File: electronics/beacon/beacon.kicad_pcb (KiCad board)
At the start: 2 copper layers, 28 x 3.5 mm, 12 parts, among them Q1 Q_NMOS_GSD, U1 ATTINY45-20XUR, U2 TPS70928DBV

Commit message: Finalize beacon schematic for initial run
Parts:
- C1: value 1uF -> 1u
- C2: value 22uF -> 22u
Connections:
- net /Rail1 renamed Net-(D2-Pad2)
- net /Rail2 renamed Net-(D2-Pad3)
- net VCC renamed Net-(C1-Pad1)
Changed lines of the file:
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@@
   )
   (net 0 "")
-  (net 1 VCC)
-  (net 2 GND)
-  (net 3 +2V8)
-  (net 4 "Net-(D1-Pad2)")
-  (net 5 "Net-(D1-Pad1)")
-  (net 6 /Rail1)
-  (net 7 /Rail2)
-  (net 8 "Net-(Q1-Pad1)")
-  (net 9 /~RST)
-  (net 10 /MISO)
-  (net 11 /MOSI)
-  (net 12 /SCK)
-  (net 13 "Net-(U2-Pad3)")
-  (net 14 "Net-(U2-Pad4)")
-  (net 15 /PB3)
-  (net 16 /PB4)
+  (net 1 GND)
+  (net 2 +2V8)
+  (net 3 "Net-(D1-Pad2)")
+  (net 4 "Net-(D1-Pad1)")
+  (net 5 "Net-(Q1-Pad1)")
+  (net 6 /~RST)
+  (net 7 /MISO)
+  (net 8 /MOSI)
+  (net 9 /SCK)
+  (net 10 "Net-(U2-Pad3)")
+  (net 11 "Net-(U2-Pad4)")
+  (net 12 /PB3)
+  (net 13 /PB4)
+  (net 14 "Net-(C1-Pad1)")
+  (net 15 "Net-(D2-Pad2)")
+  (net 16 "Net-(D2-Pad3)")
   (net_class Default "This is the default net class."
     (clearance 0.2)
@@
     (add_net /PB3)
     (add_net /PB4)
-    (add_net /Rail1)
-    (add_net /Rail2)
     (add_net /SCK)
     (add_net /~RST)
     (add_net GND)
+    (add_net "Net-(C1-Pad1)")
     (add_net "Net-(D1-Pad1)")
     (add_net "Net-(D1-Pad2)")
+    (add_net "Net-(D2-Pad2)")
+    (add_net "Net-(D2-Pad3)")
     (add_net "Net-(Q1-Pad1)")
     (add_net "Net-(U2-Pad3)")
     (add_net "Net-(U2-Pad4)")
-    (add_net VCC)
   )
   (module Housings_SSOP:TSSOP-8_4.4x3mm_Pitch0.65mm (layer B.Cu)
@@
     (fp_line (start -2.325 1.525) (end -3.675 1.525) (layer B.SilkS) (width 0.15))
     (pad 1 smd rect (at -2.95 0.975) (size 1.45 0.45) (layers B.Cu B.Paste B.Mask)
-      (net 9 /~RST))
+      (net 6 /~RST))
     (pad 2 smd rect (at -2.95 0.325) (size 1.45 0.45) (layers B.Cu B.Paste B.Mask)
-      (net 15 /PB3))
+      (net 12 /PB3))
     (pad 3 smd rect (at -2.95 -0.325) (size 1.45 0.45) (layers B.Cu B.Paste B.Mask)
-      (net 16 /PB4))
+      (net 13 /PB4))
     (pad 4 smd rect (at -2.95 -0.975) (size 1.45 0.45) (layers B.Cu B.Paste B.Mask)
-      (net 2 GND))
+      (net 1 GND))
     (pad 5 smd rect (at 2.95 -0.975) (size 1.45 0.45) (layers B.Cu B.Paste B.Mask)
-      (net 11 /MOSI))
+      (net 8 /MOSI))
     (pad 6 smd rect (at 2.95 -0.325) (size 1.45 0.45) (layers B.Cu B.Paste B.Mask)
-      (net 10 /MISO))
+      (net 7 /MISO))
     (pad 7 smd rect (at 2.95 0.325) (size 1.45 0.45) (layers B.Cu B.Paste B.Mask)
-      (net 12 /SCK))
+      (net 9 /SCK))
     (pad 8 smd rect (at 2.95 0.975) (size 1.45 0.45) (layers B.Cu B.Paste B.Mask)
-      (net 3 +2V8))
+      (net 2 +2V8))
     (model Housings_SSOP.3dshapes/TSSOP-8_4.4x3mm_Pitch0.65mm.wrl
       (at (xyz 0 0 0))
@@
     (fp_line (start -0.5 0.675) (end 0.5 0.675) (layer B.SilkS) (width 0.15))
     (pad 1 smd rect (at -1.1 0 270) (size 1.2 0.9) (layers B.Cu B.Paste B.Mask)
-      (net 3 +2V8))
+      (net 2 +2V8))
     (pad 2 smd rect (at 1.1 0 270) (size 1.2 0.9) (layers B.Cu B.Paste B.Mask)
-      (net 9 /~RST))
+      (net 6 /~RST))
     (model Resistors_SMD.3dshapes/R_0603_HandSoldering.wrl
       (at (xyz 0 0 0))
@@
       (effects (font (size 1 1) (thickness 0.15)))
     )
-    (fp_text value 1uF (at 0 1.5 270) (layer F.Fab)
+    (fp_text value 1u (at 0 1.5 270) (layer F.Fab)
       (effects (font (size 1 1) (thickness 0.15)))
     )
@@
     (fp_line (start 1.8 0.65) (end -1.8 0.65) (layer F.CrtYd) (width 0.05))
     (pad 1 smd rect (at -0.95 0 270) (size 1.2 0.75) (layers F.Cu F.Paste F.Mask)
-      (net 1 VCC))
+      (net 14 "Net-(C1-Pad1)"))
     (pad 2 smd rect (at 0.95 0 270) (size 1.2 0.75) (layers F.Cu F.Paste F.Mask)
-      (net 2 GND))
+      (net 1 GND))
     (model Capacitors_SMD.3dshapes/C_0603.wrl
       (at (xyz 0 0 0))
@@
       (effects (font (size 1 1) (thickness 0.15)))
     )
-    (fp_text value 22uF (at 0 1.5 270) (layer F.Fab)
+    (fp_text value 22u (at 0 1.5 270) (layer F.Fab)
       (effects (font (size 1 1) (thickness 0.15)))
     )
@@
     (fp_line (start 1.8 0.65) (end -1.8 0.65) (layer F.CrtYd) (width 0.05))
     (pad 1 smd rect (at -0.95 0 270) (size 1.2 0.75) (layers F.Cu F.Paste F.Mask)
-      (net 3 +2V8))
+      (net 2 +2V8))
     (pad 2 smd rect (at 0.95 0 270) (size 1.2 0.75) (layers F.Cu F.Paste F.Mask)
-      (net 2 GND))
+      (net 1 GND))
     (model Capacitors_SMD.3dshapes/C_0603.wrl
       (at (xyz 0 0 0))
@@
     (fp_line (start -1.45 -0.65) (end 1.45 -0.65) (layer F.CrtYd) (width 0.05))
     (pad 2 smd rect (at 0.8 0 270) (size 0.8 0.8) (layers F.Cu F.Paste F.Mask)
-      (net 4 "Net-(D1-Pad2)"))
+      (net 3 "Net-(D1-Pad2)"))
     (pad 1 smd rect (at -0.8 0 270) (size 0.8 0.8) (layers F.Cu F.Paste F.Mask)
-      (net 5 "Net-(D1-Pad1)"))
+      (net 4 "Net-(D1-Pad1)"))
     (model LEDs.3dshapes/LED_0603.wrl
       (at (xyz 0 0 0))
@@
     (fp_line (start -2.05 1.75) (end -2.05 -1.75) (layer F.CrtYd) (width 0.05))
     (pad 1 smd rect (at -1.1 -0.77 270) (size 1.2 1.4) (layers F.Cu F.Paste F.Mask)
-      (net 2 GND))
+      (net 1 GND))
     (pad 2 smd rect (at -1.1 0.95 270) (size 1 1.4) (layers F.Cu F.Paste F.Mask)
-      (net 6 /Rail1))
+      (net 15 "Net-(D2-Pad2)"))
     (pad 3 smd rect (at 1.1 0.95 270) (size 1 1.4) (layers F.Cu F.Paste F.Mask)
-      (net 7 /Rail2))
+      (net 16 "Net-(D2-Pad3)"))
     (pad 4 smd rect (at 1.1 -0.95 270) (size 1 1.4) (layers F.Cu F.Paste F.Mask)
-      (net 1 VCC))
+      (net 14 "Net-(C1-Pad1)"))
     (model TO_SOT_Packages_SMD.3dshapes/SOT-143.wrl
       (at (xyz 0 -0 0))
@@
     (fp_line (start 0.76 -1.58) (end -0.7 -1.58) (layer B.SilkS) (width 0.12))
     (pad 1 smd rect (at -1 0.95) (size 0.9 0.8) (layers B.Cu B.Paste B.Mask)
-      (net 8 "Net-(Q1-Pad1)"))
+      (net 5 "Net-(Q1-Pad1)"))
     (pad 2 smd rect (at -1 -0.95) (size 0.9 0.8) (layers B.Cu B.Paste B.Mask)
-      (net 2 GND))
+      (net 1 GND))
     (pad 3 smd rect (at 1 0) (size 0.9 0.8) (layers B.Cu B.Paste B.Mask)
-      (net 5 "Net-(D1-Pad1)"))
+      (net 4 "Net-(D1-Pad1)"))
     (model TO_SOT_Packages_SMD.3dshapes/SOT-23.wrl
       (at (xyz 0 0 0))
@@
     (fp_line (start -0.5 0.675) (end 0.5 0.675) (layer B.SilkS) (width 0.15))
     (pad 1 smd rect (at -1.1 0 270) (size 1.2 0.9) (layers B.Cu B.Paste B.Mask)
-      (net 10 /MISO))
+      (net 7 /MISO))
     (pad 2 smd rect (at 1.1 0 270) (size 1.2 0.9) (layers B.Cu B.Paste B.Mask)
-      (net 8 "Net-(Q1-Pad1)"))
+      (net 5 "Net-(Q1-Pad1)"))
     (model Resistors_SMD.3dshapes/R_0603_HandSoldering.wrl
       (at (xyz 0 0 0))
@@
     (fp_line (start -0.5 0.675) (end 0.5 0.675) (layer B.SilkS) (width 0.15))
     (pad 1 smd rect (at -1.1 0 90) (size 1.2 0.9) (layers B.Cu B.Paste B.Mask)
-      (net 8 "Net-(Q1-Pad1)"))
+      (net 5 "Net-(Q1-Pad1)"))
     (pad 2 smd rect (at 1.1 0 90) (size 1.2 0.9) (layers B.Cu B.Paste B.Mask)
-      (net 2 GND))
+      (net 1 GND))
     (model Resistors_SMD.3dshapes/R_0603_HandSoldering.wrl
       (at (xyz 0 0 0))
@@
     (fp_line (start -0.5 0.675) (end 0.5 0.675) (layer B.SilkS) (width 0.15))
     (pad 1 smd rect (at -1.1 0 270) (size 1.2 0.9) (layers B.Cu B.Paste B.Mask)
-      (net 3 +2V8))
+      (net 2 +2V8))
     (pad 2 smd rect (at 1.1 0 270) (size 1.2 0.9) (layers B.Cu B.Paste B.Mask)
-      (net 4 "Net-(D1-Pad2)"))
+      (net 3 "Net-(D1-Pad2)"))
     (model Resistors_SMD.3dshapes/R_0603_HandSoldering.wrl
       (at (xyz 0 0 0))
@@
     (fp_line (start 0.9 -1.55) (end 0.9 1.55) (layer F.Fab) (width 0.1))
     (pad 1 smd rect (at -1.1 -0.95) (size 1.06 0.65) (layers F.Cu F.Paste F.Mask)
-      (net 1 VCC))
+      (net 14 "Net-(C1-Pad1)"))
     (pad 2 smd rect (at -1.1 0) (size 1.06 0.65) (layers F.Cu F.Paste F.Mask)
-      (net 2 GND))
+      (net 1 GND))
     (pad 3 smd rect (at -1.1 0.95) (size 1.06 0.65) (layers F.Cu F.Paste F.Mask)
-      (net 13 "Net-(U2-Pad3)"))
+      (net 10 "Net-(U2-Pad3)"))
     (pad 4 smd rect (at 1.1 0.95) (size 1.06 0.65) (layers F.Cu F.Paste F.Mask)
-      (net 14 "Net-(U2-Pad4)"))
+      (net 11 "Net-(U2-Pad4)"))
     (pad 5 smd rect (at 1.1 -0.95) (size 1.06 0.65) (layers F.Cu F.Paste F.Mask)
-      (net 3 +2V8))
+      (net 2 +2V8))
     (model TO_SOT_Packages_SMD.3dshapes/SOT-23-5.wrl
       (at (xyz 0 0 0))
@@
     (fp_line (start -0.5 0.675) (end 0.5 0.675) (layer B.SilkS) (width 0.15))
     (pad 1 smd rect (at -1.1 0 90) (size 1.2 0.9) (layers B.Cu B.Paste B.Mask)
-      (net 4 "Net-(D1-Pad2)"))
+      (net 3 "Net-(D1-Pad2)"))
     (pad 2 smd rect (at 1.1 0 90) (size 1.2 0.9) (layers B.Cu B.Paste B.Mask)
-      (net 5 "Net-(D1-Pad1)"))
+      (net 4 "Net-(D1-Pad1)"))
     (model Resistors_SMD.3dshapes/R_0603_HandSoldering.wrl
       (at (xyz 0 0 0))

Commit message: electronics: beacon: WIP 3.5x28 board layout
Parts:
- added J1: CONN_02X02, bcan:Edge_Connector_2x02_Pitch2.54mm_SMD, F.Cu at (136.0, 105.0)
- added J2: CONN_02X02, bcan:Edge_Connector_2x02_Pitch2.54mm_SMD, F.Cu at (164.0, 105.0)
- added J3: Rails, bcan:HO_Rail_2_Length3.5mm_Width3mm, F.Cu at (150.0, 105.0)
- C1, C2: footprint Capacitors_SMD:C_0603_HandSoldering -> Capacitors_SMD:C_0603; moved to B.Cu
- D2: value D_Bridge_-AA+ -> Rectifier; moved to B.Cu
- Q1: moved to F.Cu
- R1: footprint Resistors_SMD:R_0603_HandSoldering -> Resistors_SMD:R_0603
- R2, R3, R4, R5: footprint Resistors_SMD:R_0603_HandSoldering -> Resistors_SMD:R_0603; moved to F.Cu
- U2: moved to B.Cu
- moved R1 17.8 mm to (158.2, 105.0), turned to 90 degrees
- moved D2 8.81 mm to (152.2, 100.0), turned to 180 degrees
- moved C2 8.75 mm to (145.2, 105.0), turned to 90 degrees
- moved U2 8.40 mm to (142.5, 105.0)
- moved C1 8.25 mm to (139.8, 105.0), turned to 90 degrees
- moved U1 8.10 mm to (153.6, 105.0), turned to 180 degrees
- moved R5 4.53 mm to (155.0, 104.5), turned to 0 degrees
- moved R3 3.64 mm to (149.0, 106.0), turned to 0 degrees
- moved Q1 3.00 mm to (152.0, 105.0)
- moved R4 2.69 mm to (155.0, 106.0), turned to 0 degrees
- moved R2 1.80 mm to (149.0, 104.0), turned to 0 degrees
- moved D1 1.00 mm to (157.0, 105.0), turned to 270 degrees
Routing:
- net +2V8: track 0.00 -> 10.1 mm, vias 0 -> 1
- net Net-(D1-Pad1): track 0.00 -> 5.47 mm
- net Net-(Q1-Pad1): track 0.00 -> 3.89 mm
- net /MISO: track 0.00 -> 3.51 mm, vias 0 -> 1
- net Net-(D1-Pad2): track 0.00 -> 3.45 mm
- net /~RST: track 0.00 -> 1.85 mm
- net GND: track 0.00 -> 1.27 mm
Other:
- net class Tight added: clearance 0.2, trace_width 0.2, via_dia 0.5, via_drill 0.3
- rule trace_min: 0.2 -> 0.16
- board text added: "57F1"

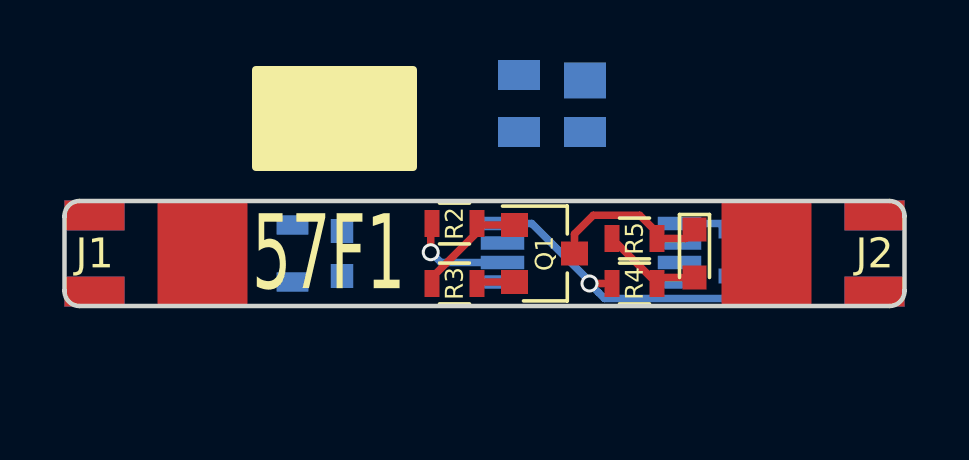
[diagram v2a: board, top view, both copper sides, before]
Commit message: electronics: beacon: Final beacon board Rev 1.0
- increase board size to fit all components
- add rail and connector footprints to library
- improve track mechanical model
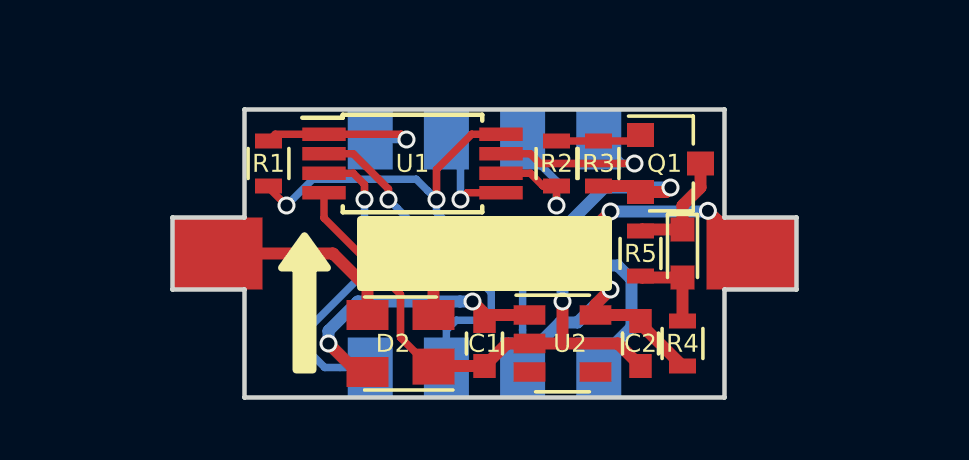
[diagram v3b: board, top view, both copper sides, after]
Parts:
- C1, C2, D2, R1, U1, U2: moved to F.Cu
- J1, J2: value CONN_02X02 -> CONN_01X04; footprint bcan:Edge_Connector_2x02_Pitch2.54mm_SMD -> bcan:Edge_Connector_1x04_Pitch2.54mm_SMD; moved to B.Cu
- J3: footprint bcan:HO_Rail_2_Length3.5mm_Width3mm -> bcan:HO_Rail_2_Length2.4mm_Width3mm
- moved R1 15.7 mm to (142.8, 102.0)
- moved J1 14.8 mm to (150.0, 100.2), turned to 90 degrees
- moved J2 14.8 mm to (150.0, 109.8), turned to 270 degrees
- moved C1 10.7 mm to (150.0, 108.0), turned to 270 degrees
- moved U2 10.5 mm to (152.6, 108.0)
- moved C2 10.4 mm to (155.2, 108.0), turned to 270 degrees
- moved D2 9.46 mm to (147.2, 108.0)
- moved U1 6.65 mm to (147.6, 102.0), turned to 0 degrees
- moved R3 6.25 mm to (153.8, 102.0), turned to 270 degrees
- moved Q1 5.16 mm to (156.2, 102.0)
- moved R2 3.94 mm to (152.4, 102.0), turned to 90 degrees
- moved R4 2.56 mm to (156.6, 108.0), turned to 90 degrees
- moved R5 0.54 mm to (155.2, 105.0), turned to 90 degrees
- moved D1 0.40 mm to (156.6, 105.0)
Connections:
- J1 pad 1: /MOSI -> /SCK
- J1 pad 2: GND -> /MISO
- J1 pad 3: /SCK -> /MOSI
- J1 pad 4: /MISO -> /~RST
- J2 pad 1: /PB3 -> /PB4
- J2 pad 2: /~RST -> /PB3
- J2 pad 3: /PB4 -> +2V8
- J2 pad 4: +2V8 -> GND
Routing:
- net GND: track 1.27 -> 31.4 mm, vias 0 -> 2
- net +2V8: track 10.1 -> 26.7 mm, vias 1 -> 3
- net Net-(D2-Pad2): track 0.00 -> 14.0 mm, vias 0 -> 2
- net /PB3: track 0.00 -> 11.3 mm, vias 0 -> 1
- net /PB4: track 0.00 -> 10.1 mm, vias 0 -> 1
- net Net-(C1-Pad1): track 0.00 -> 9.72 mm, vias 0 -> 2
- net Net-(D2-Pad3): track 0.00 -> 6.38 mm
- net /SCK: track 0.00 -> 6.11 mm, vias 0 -> 1
- net /~RST: track 1.85 -> 5.98 mm, vias 0 -> 1
- net /MOSI: track 0.00 -> 3.64 mm, vias 0 -> 1
- net /MISO: track 3.51 -> 5.34 mm
- net Net-(D1-Pad1): track 5.47 -> 3.87 mm
- net Net-(Q1-Pad1): track 3.89 -> 2.88 mm
- net Net-(D1-Pad2): track 3.45 -> 2.87 mm
- added copper zone on B.Cu, net GND
- added copper zone on F.Cu, net GND
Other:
- board size 28 x 3.5 mm -> 20.8 x 9.6 mm
- net class Power added: clearance 0.2, trace_width 0.4, via_dia 0.6, via_drill 0.4
- board text added: "3"
- board text added: "4"
- board text added: "I"
- board text added: "L"
- board text added: "O"
- board text added: "R"
- board text added: "Rev 1.0"
- board text added: "S"
- board text added: "V"
- board text removed: "57F1"
